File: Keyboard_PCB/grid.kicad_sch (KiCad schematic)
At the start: 136 parts, among them SW10 7, SW11 8, SW12 9, SW13 0, SW14 -, SW15 =, SW16 <-, SW17 DEL, SW18 TAB, SW19 Q, SW20 W, SW21 E, SW22 R, SW23 T, SW24 Y, SW25 U, SW26 I, SW27 O, SW28 P, SW29 [, SW3 ESC, SW30 ], SW31 \, SW32 HOME, SW34 CAPS, SW35 A, SW36 S, SW37 D, SW38 F, SW39 G, SW4 1, SW40 H, SW41 J, SW42 K, SW43 L, SW44 ;, SW45 ', SW46 ENTER, SW47 PG_U, SW48 SHIFT, SW49 Z, SW5 2, SW50 X, SW51 C, SW52 V, SW53 B, SW54 N, SW55 M, SW56 ,, SW57 ., SW58 /, SW59 SHIFT, SW6 3, SW60 UP, SW61 PG_D, SW62 CTRL, SW63 CODE, SW64 ALT, SW65 SPACE, SW66 ALT, SW67 CODE, SW68 CTRL, SW69 LEFT, SW7 4, SW70 DOWN, SW71 RIGHT, SW8 5, SW9 6

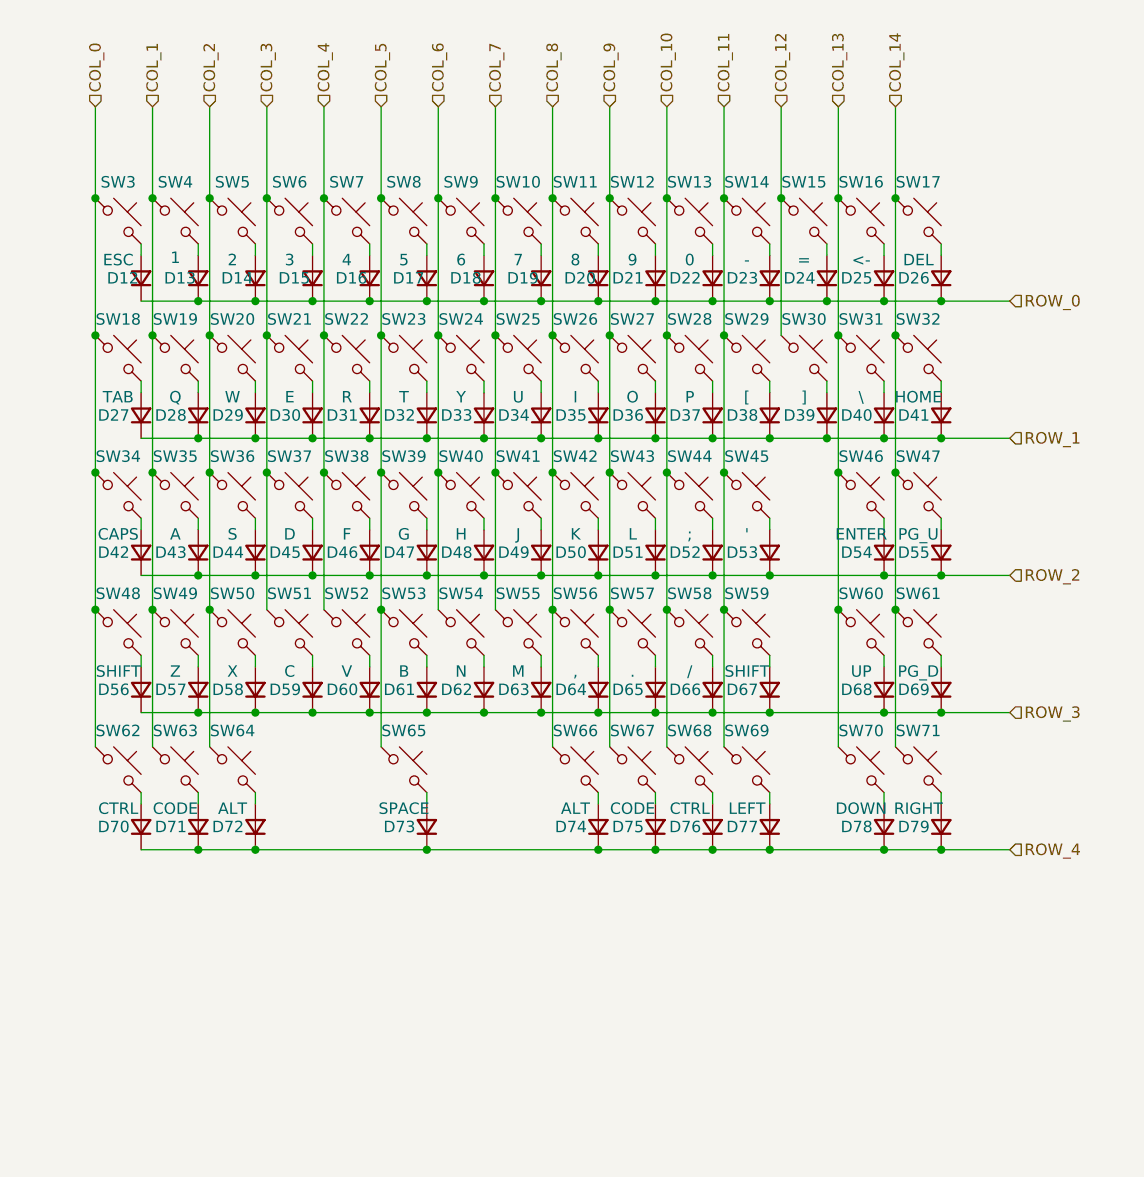
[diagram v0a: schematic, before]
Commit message: Keypad schematic progress
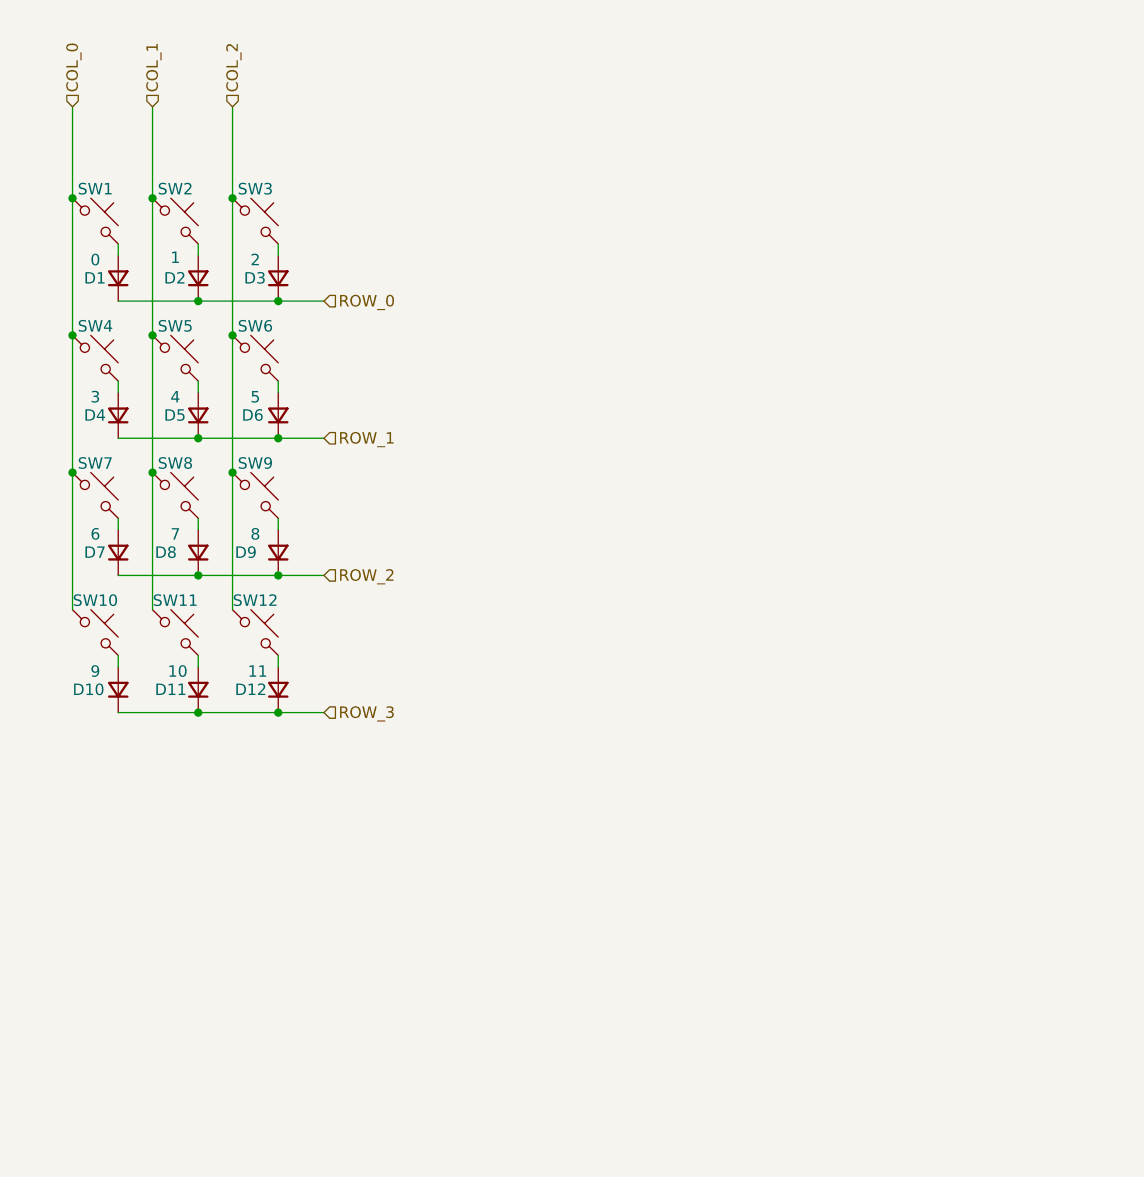
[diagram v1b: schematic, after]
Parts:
- removed D15, D16, D17, D18, D19, D20, D21, D22, D23, D24, D25, D26, D30, D31, D32, D33, D34, D35, D36, D37, D38, D39, D40, D41, D45, D46, D47, D48, D49, D50, D51, D52, D53, D54, D55, D59, D60, D61, D62, D63, D64, D65, D66, D67, D68, D69, D70, D71, D72, D73, D74, D75, D76, D77, D78, D79: D_Small, Diode_SMD:D_SOD-323, symbol Device:D_Small
- removed SW10: 7, Keyboard_Switch:SW_Cherry_MX1A_1.00u_PCB, symbol Switch:SW_Push_45deg
- removed SW11: 8, Keyboard_Switch:SW_Cherry_MX1A_1.00u_PCB, symbol Switch:SW_Push_45deg
- removed SW12: 9, Keyboard_Switch:SW_Cherry_MX1A_1.00u_PCB, symbol Switch:SW_Push_45deg
- removed SW13: 0, Keyboard_Switch:SW_Cherry_MX1A_1.00u_PCB, symbol Switch:SW_Push_45deg
- removed SW14: -, Keyboard_Switch:SW_Cherry_MX1A_1.00u_PCB, symbol Switch:SW_Push_45deg
- removed SW15: =, Keyboard_Switch:SW_Cherry_MX1A_1.00u_PCB, symbol Switch:SW_Push_45deg
- removed SW16: <-, Keyboard_Switch:SW_Cherry_MX1A_2.00u_PCB, symbol Switch:SW_Push_45deg
- removed SW17: DEL, Keyboard_Switch:SW_Cherry_MX1A_1.00u_PCB, symbol Switch:SW_Push_45deg
- removed SW21: E, Keyboard_Switch:SW_Cherry_MX1A_1.00u_PCB, symbol Switch:SW_Push_45deg
- removed SW22: R, Keyboard_Switch:SW_Cherry_MX1A_1.00u_PCB, symbol Switch:SW_Push_45deg
- removed SW23: T, Keyboard_Switch:SW_Cherry_MX1A_1.00u_PCB, symbol Switch:SW_Push_45deg
- removed SW24: Y, Keyboard_Switch:SW_Cherry_MX1A_1.00u_PCB, symbol Switch:SW_Push_45deg
- removed SW25: U, Keyboard_Switch:SW_Cherry_MX1A_1.00u_PCB, symbol Switch:SW_Push_45deg
- removed SW26: I, Keyboard_Switch:SW_Cherry_MX1A_1.00u_PCB, symbol Switch:SW_Push_45deg
- removed SW27: O, Keyboard_Switch:SW_Cherry_MX1A_1.00u_PCB, symbol Switch:SW_Push_45deg
- removed SW28: P, Keyboard_Switch:SW_Cherry_MX1A_1.00u_PCB, symbol Switch:SW_Push_45deg
- removed SW29: [, Keyboard_Switch:SW_Cherry_MX1A_1.00u_PCB, symbol Switch:SW_Push_45deg
- removed SW30: ], Keyboard_Switch:SW_Cherry_MX1A_1.00u_PCB, symbol Switch:SW_Push_45deg
- removed SW31: \, Keyboard_Switch:SW_Cherry_MX1A_1.50u_PCB, symbol Switch:SW_Push_45deg
- removed SW32: HOME, Keyboard_Switch:SW_Cherry_MX1A_1.00u_PCB, symbol Switch:SW_Push_45deg
- removed SW37: D, Keyboard_Switch:SW_Cherry_MX1A_1.00u_PCB, symbol Switch:SW_Push_45deg
- removed SW38: F, Keyboard_Switch:SW_Cherry_MX1A_1.00u_PCB, symbol Switch:SW_Push_45deg
- removed SW39: G, Keyboard_Switch:SW_Cherry_MX1A_1.00u_PCB, symbol Switch:SW_Push_45deg
- removed SW40: H, Keyboard_Switch:SW_Cherry_MX1A_1.00u_PCB, symbol Switch:SW_Push_45deg
- removed SW41: J, Keyboard_Switch:SW_Cherry_MX1A_1.00u_PCB, symbol Switch:SW_Push_45deg
- removed SW42: K, Keyboard_Switch:SW_Cherry_MX1A_1.00u_PCB, symbol Switch:SW_Push_45deg
- removed SW43: L, Keyboard_Switch:SW_Cherry_MX1A_1.00u_PCB, symbol Switch:SW_Push_45deg
- removed SW44: ;, Keyboard_Switch:SW_Cherry_MX1A_1.00u_PCB, symbol Switch:SW_Push_45deg
- removed SW45: ', Keyboard_Switch:SW_Cherry_MX1A_1.00u_PCB, symbol Switch:SW_Push_45deg
- removed SW46: ENTER, Keyboard_Switch:SW_Cherry_MX1A_2.25u_PCB, symbol Switch:SW_Push_45deg
- removed SW47: PG_U, Keyboard_Switch:SW_Cherry_MX1A_1.00u_PCB, symbol Switch:SW_Push_45deg
- removed SW51: C, Keyboard_Switch:SW_Cherry_MX1A_1.00u_PCB, symbol Switch:SW_Push_45deg
- removed SW52: V, Keyboard_Switch:SW_Cherry_MX1A_1.00u_PCB, symbol Switch:SW_Push_45deg
- removed SW53: B, Keyboard_Switch:SW_Cherry_MX1A_1.00u_PCB, symbol Switch:SW_Push_45deg
- removed SW54: N, Keyboard_Switch:SW_Cherry_MX1A_1.00u_PCB, symbol Switch:SW_Push_45deg
- removed SW55: M, Keyboard_Switch:SW_Cherry_MX1A_1.00u_PCB, symbol Switch:SW_Push_45deg
- removed SW56: ,, Keyboard_Switch:SW_Cherry_MX1A_1.00u_PCB, symbol Switch:SW_Push_45deg
- removed SW57: ., Keyboard_Switch:SW_Cherry_MX1A_1.00u_PCB, symbol Switch:SW_Push_45deg
- removed SW58: /, Keyboard_Switch:SW_Cherry_MX1A_1.00u_PCB, symbol Switch:SW_Push_45deg
- removed SW59: SHIFT, Keyboard_Switch:SW_Cherry_MX1A_1.75u_PCB, symbol Switch:SW_Push_45deg
- removed SW6: 3, Keyboard_Switch:SW_Cherry_MX1A_1.00u_PCB, symbol Switch:SW_Push_45deg
- removed SW60: UP, Keyboard_Switch:SW_Cherry_MX1A_1.00u_PCB, symbol Switch:SW_Push_45deg
- removed SW61: PG_D, Keyboard_Switch:SW_Cherry_MX1A_1.00u_PCB, symbol Switch:SW_Push_45deg
- removed SW62: CTRL, Keyboard_Switch:SW_Cherry_MX1A_1.25u_PCB, symbol Switch:SW_Push_45deg
- removed SW63: CODE, Keyboard_Switch:SW_Cherry_MX1A_1.25u_PCB, symbol Switch:SW_Push_45deg
- removed SW64: ALT, Keyboard_Switch:SW_Cherry_MX1A_1.25u_PCB, symbol Switch:SW_Push_45deg
- removed SW65: SPACE, Keyboard_Switch:SW_Cherry_MX1A_6.25u_PCB, symbol Switch:SW_Push_45deg
- removed SW66: ALT, Keyboard_Switch:SW_Cherry_MX1A_1.00u_PCB, symbol Switch:SW_Push_45deg
- removed SW67: CODE, Keyboard_Switch:SW_Cherry_MX1A_1.00u_PCB, symbol Switch:SW_Push_45deg
- removed SW68: CTRL, Keyboard_Switch:SW_Cherry_MX1A_1.00u_PCB, symbol Switch:SW_Push_45deg
- removed SW69: LEFT, Keyboard_Switch:SW_Cherry_MX1A_1.00u_PCB, symbol Switch:SW_Push_45deg
- removed SW7: 4, Keyboard_Switch:SW_Cherry_MX1A_1.00u_PCB, symbol Switch:SW_Push_45deg
- removed SW70: DOWN, Keyboard_Switch:SW_Cherry_MX1A_1.00u_PCB, symbol Switch:SW_Push_45deg
- removed SW71: RIGHT, Keyboard_Switch:SW_Cherry_MX1A_1.00u_PCB, symbol Switch:SW_Push_45deg
- removed SW8: 5, Keyboard_Switch:SW_Cherry_MX1A_1.00u_PCB, symbol Switch:SW_Push_45deg
- removed SW9: 6, Keyboard_Switch:SW_Cherry_MX1A_1.00u_PCB, symbol Switch:SW_Push_45deg
- SW1: renamed from SW3; value ESC -> 0; footprint Keyboard_Switch:SW_Cherry_MX1A_1.00u_PCB -> Button_Switch_Keyboard:SW_Cherry_MX_1.00u_PCB
- SW10: renamed from SW48; value SHIFT -> 9; footprint Keyboard_Switch:SW_Cherry_MX1A_2.25u_PCB -> Button_Switch_Keyboard:SW_Cherry_MX_1.00u_PCB
- SW11: renamed from SW49; value Z -> 10; footprint Keyboard_Switch:SW_Cherry_MX1A_1.00u_PCB -> Button_Switch_Keyboard:SW_Cherry_MX_1.00u_PCB
- SW12: renamed from SW50; value X -> 11; footprint Keyboard_Switch:SW_Cherry_MX1A_1.00u_PCB -> Button_Switch_Keyboard:SW_Cherry_MX_1.00u_PCB
- SW2: renamed from SW4; footprint Keyboard_Switch:SW_Cherry_MX1A_1.00u_PCB -> Button_Switch_Keyboard:SW_Cherry_MX_1.00u_PCB
- SW3: renamed from SW5; footprint Keyboard_Switch:SW_Cherry_MX1A_1.00u_PCB -> Button_Switch_Keyboard:SW_Cherry_MX_1.00u_PCB
- SW4: renamed from SW18; value TAB -> 3; footprint Keyboard_Switch:SW_Cherry_MX1A_1.50u_PCB -> Button_Switch_Keyboard:SW_Cherry_MX_1.00u_PCB
- SW5: renamed from SW19; value Q -> 4; footprint Keyboard_Switch:SW_Cherry_MX1A_1.00u_PCB -> Button_Switch_Keyboard:SW_Cherry_MX_1.00u_PCB
- SW6: renamed from SW20; value W -> 5; footprint Keyboard_Switch:SW_Cherry_MX1A_1.00u_PCB -> Button_Switch_Keyboard:SW_Cherry_MX_1.00u_PCB
- SW7: renamed from SW34; value CAPS -> 6; footprint Keyboard_Switch:SW_Cherry_MX1A_1.75u_PCB -> Button_Switch_Keyboard:SW_Cherry_MX_1.00u_PCB
- SW8: renamed from SW35; value A -> 7; footprint Keyboard_Switch:SW_Cherry_MX1A_1.00u_PCB -> Button_Switch_Keyboard:SW_Cherry_MX_1.00u_PCB
- SW9: renamed from SW36; value S -> 8; footprint Keyboard_Switch:SW_Cherry_MX1A_1.00u_PCB -> Button_Switch_Keyboard:SW_Cherry_MX_1.00u_PCB
- renumbered D12 to D1, D56 to D10, D57 to D11, D58 to D12, D13 to D2, D14 to D3, D27 to D4, D28 to D5, D29 to D6, D42 to D7, D43 to D8, D44 to D9
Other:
- moved on the sheet: D1, D10, D12, D3, D4, D6, D7, D9, SW1, SW10, SW12, SW3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

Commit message: STM32U385 pin assignment progress
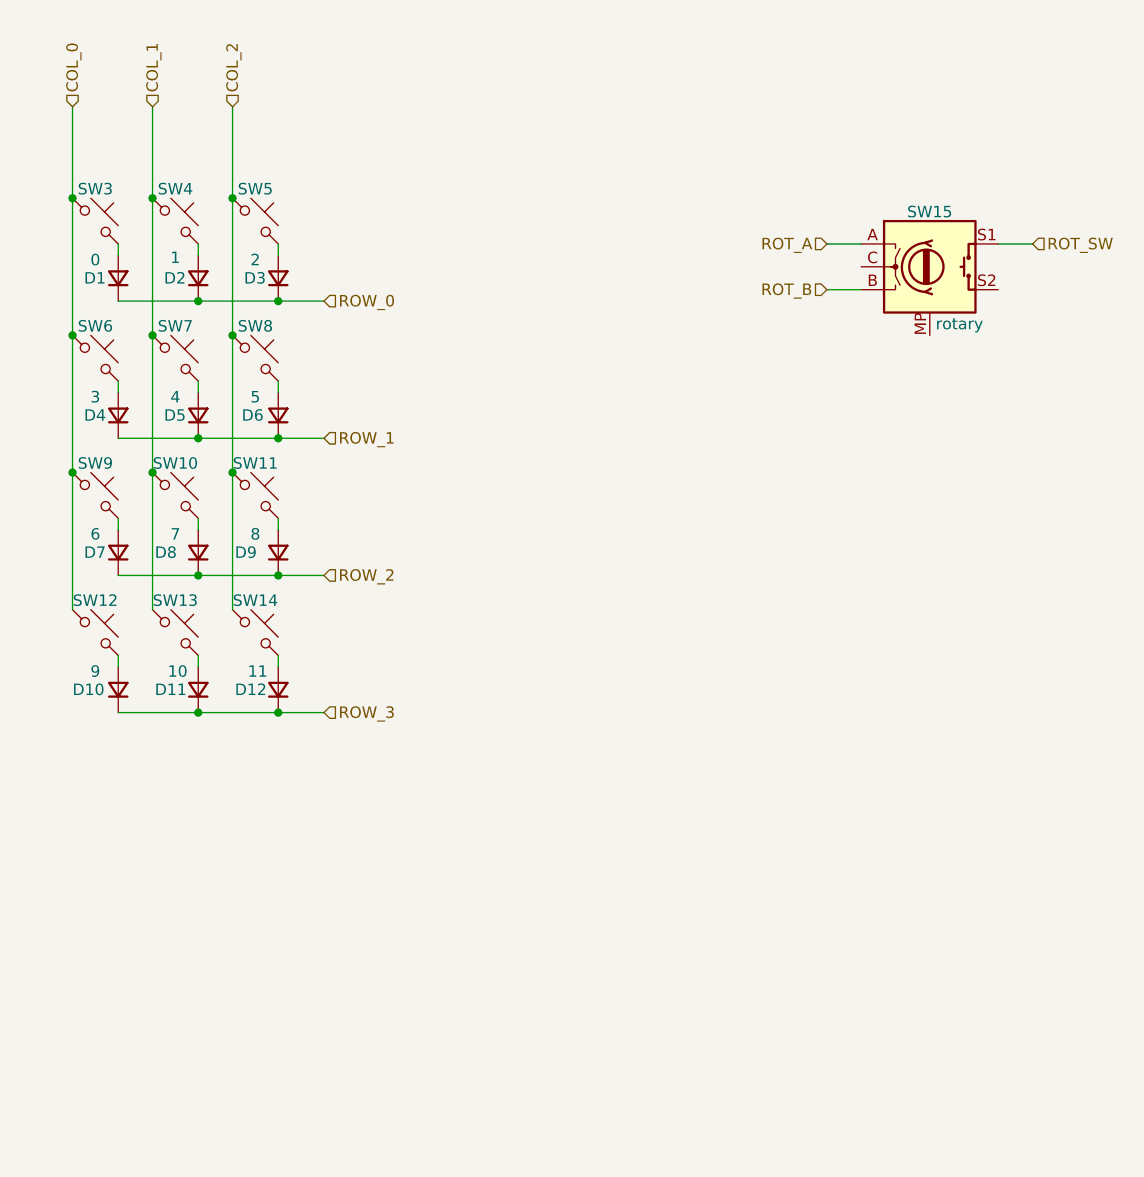
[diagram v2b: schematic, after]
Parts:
- added SW15: rotary, symbol Device:RotaryEncoder_Switch_MP
- renumbered SW8 to SW10, SW9 to SW11, SW10 to SW12, SW11 to SW13, SW12 to SW14, SW1 to SW3, SW2 to SW4, SW3 to SW5, SW4 to SW6, SW5 to SW7, SW6 to SW8, SW7 to SW9
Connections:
- new net ROT_A: SW15.A
- new net ROT_B: SW15.B
- new net ROT_SW: SW15.S1
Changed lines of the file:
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@@
+	(wire
+		(pts
+			(xy 167.64 66.04) (xy 163.83 66.04)
+		)
+		(stroke
+			(width 0)
+			(type default)
+		)
+	)
 	(wire
 		(pts
@@
 	(wire
 		(pts
+			(xy 144.78 71.12) (xy 148.59 71.12)
+		)
+		(stroke
+			(width 0)
+			(type default)
+		)
+	)
+	(wire
+		(pts
 			(xy 60.96 60.96) (xy 60.96 76.2)
 		)
@@
 	(wire
 		(pts
+			(xy 144.78 66.04) (xy 148.59 66.04)
+		)
+		(stroke
+			(width 0)
+			(type default)
+		)
+	)
+	(wire
+		(pts
 			(xy 83.82 67.31) (xy 83.82 66.04)
 		)
@@
 			(width 0)
 			(type default)
+		)
+	)
+	(hierarchical_label "ROT_B"
+		(shape input)
+		(at 144.78 71.12 180)
+		(effects
+			(font
+				(size 1.27 1.27)
+			)
+			(justify right)
 		)
 	)
@@
 		)
 	)
+	(hierarchical_label "ROT_SW"
+		(shape input)
+		(at 167.64 66.04 0)
+		(effects
+			(font
+				(size 1.27 1.27)
+			)
+			(justify left)
+		)
+	)
+	(hierarchical_label "ROT_A"
+		(shape input)
+		(at 144.78 66.04 180)
+		(effects
+			(font
+				(size 1.27 1.27)
+			)
+			(justify right)
+		)
+	)
 	(hierarchical_label "ROW_3"
 		(shape input)
@@
 		(on_board yes)
 		(dnp no)
-		(property "Reference" "SW4"
+		(property "Reference" "SW6"
 			(at 63.5 75.184 0)
 			(effects
@@
 			(project "Keyboard_PCB"
 				(path "/dd51e792-c76c-4d43-96de-494177f3b593/2efb7614-f68d-465d-9514-3e61f2b99fcc"
-					(reference "SW4")
+					(reference "SW6")
 					(unit 1)
 				)
@@
 		(on_board yes)
 		(dnp no)
-		(property "Reference" "SW12"
+		(property "Reference" "SW14"
 			(at 81.28 105.664 0)
 			(effects
@@
 			(project "Keyboard_PCB"
 				(path "/dd51e792-c76c-4d43-96de-494177f3b593/2efb7614-f68d-465d-9514-3e61f2b99fcc"
-					(reference "SW12")
+					(reference "SW14")
 					(unit 1)
 				)
@@
 		(on_board yes)
 		(dnp no)
-		(property "Reference" "SW5"
+		(property "Reference" "SW7"
 			(at 72.39 75.184 0)
 			(effects
@@
 			(project "Keyboard_PCB"
 				(path "/dd51e792-c76c-4d43-96de-494177f3b593/2efb7614-f68d-465d-9514-3e61f2b99fcc"
-					(reference "SW5")
+					(reference "SW7")
 					(unit 1)
 				)
@@
 		(on_board yes)
 		(dnp no)
-		(property "Reference" "SW3"
+		(property "Reference" "SW5"
 			(at 81.28 59.944 0)
 			(effects
@@
 			(project "Keyboard_PCB"
 				(path "/dd51e792-c76c-4d43-96de-494177f3b593/2efb7614-f68d-465d-9514-3e61f2b99fcc"
-					(reference "SW3")
+					(reference "SW5")
 					(unit 1)
 				)
@@
 		(on_board yes)
 		(dnp no)
-		(property "Reference" "SW7"
+		(property "Reference" "SW9"
 			(at 63.5 90.424 0)
 			(effects
@@
 			(project "Keyboard_PCB"
 				(path "/dd51e792-c76c-4d43-96de-494177f3b593/2efb7614-f68d-465d-9514-3e61f2b99fcc"
-					(reference "SW7")
+					(reference "SW9")
 					(unit 1)
 				)
@@
 		(on_board yes)
 		(dnp no)
-		(property "Reference" "SW9"
+		(property "Reference" "SW11"
 			(at 81.28 90.424 0)
 			(effects
@@
 			(project "Keyboard_PCB"
 				(path "/dd51e792-c76c-4d43-96de-494177f3b593/2efb7614-f68d-465d-9514-3e61f2b99fcc"
-					(reference "SW9")
+					(reference "SW11")
 					(unit 1)
 				)
@@
 		(on_board yes)
 		(dnp no)
-		(property "Reference" "SW1"
+		(property "Reference" "SW3"
 			(at 63.5 59.944 0)
 			(effects
@@
 			(project "Keyboard_PCB"
 				(path "/dd51e792-c76c-4d43-96de-494177f3b593/2efb7614-f68d-465d-9514-3e61f2b99fcc"
-					(reference "SW1")
+					(reference "SW3")
 					(unit 1)
 				)
@@
 		(on_board yes)
 		(dnp no)
-		(property "Reference" "SW6"
+		(property "Reference" "SW8"
 			(at 81.28 75.184 0)
 			(effects
@@
 			(project "Keyboard_PCB"
 				(path "/dd51e792-c76c-4d43-96de-494177f3b593/2efb7614-f68d-465d-9514-3e61f2b99fcc"
-					(reference "SW6")
+					(reference "SW8")
 					(unit 1)
 				)
@@
 		(on_board yes)
 		(dnp no)
-		(property "Reference" "SW10"
+		(property "Reference" "SW12"
 			(at 63.5 105.664 0)
 			(effects
@@
 			(project "Keyboard_PCB"
 				(path "/dd51e792-c76c-4d43-96de-494177f3b593/2efb7614-f68d-465d-9514-3e61f2b99fcc"
-					(reference "SW10")
+					(reference "SW12")
 					(unit 1)
 				)
@@
 		(on_board yes)
 		(dnp no)
-		(property "Reference" "SW8"
+		(property "Reference" "SW10"
 			(at 72.39 90.424 0)
 			(effects
@@
 			(project "Keyboard_PCB"
 				(path "/dd51e792-c76c-4d43-96de-494177f3b593/2efb7614-f68d-465d-9514-3e61f2b99fcc"
-					(reference "SW8")
+					(reference "SW10")
 					(unit 1)
 				)
@@
 		(on_board yes)
 		(dnp no)
-		(property "Reference" "SW11"
+		(property "Reference" "SW13"
 			(at 72.39 105.664 0)
 			(effects
@@
 			(project "Keyboard_PCB"
 				(path "/dd51e792-c76c-4d43-96de-494177f3b593/2efb7614-f68d-465d-9514-3e61f2b99fcc"
-					(reference "SW11")
+					(reference "SW13")
 					(unit 1)
 				)
@@
 		(on_board yes)
 		(dnp no)
-		(property "Reference" "SW2"
+		(property "Reference" "SW4"
 			(at 72.39 59.944 0)
 			(effects
@@
 			(project "Keyboard_PCB"
 				(path "/dd51e792-c76c-4d43-96de-494177f3b593/2efb7614-f68d-465d-9514-3e61f2b99fcc"
-					(reference "SW2")
-					(unit 1)
-				)
+					(reference "SW4")
+					(unit 1)
+				)
+			)
+		)
+	)
+	(symbol
+		(lib_id "Device:RotaryEncoder_Switch_MP")
+		(at 156.21 68.58 0)
+		(unit 1)
+		(exclude_from_sim no)
+		(in_bom yes)
+		(on_board yes)
+		(dnp no)
+		(property "Reference" "SW15"
+			(at 156.21 62.484 0)
+			(effects
+				(font
+					(size 1.27 1.27)
+				)
+			)
+		)
+		(property "Value" "rotary"
+			(at 159.512 74.93 0)
+			(effects
+				(font
+					(size 1.27 1.27)
+				)
+			)
+		)
+		(property "Footprint" ""
+			(at 152.4 64.516 0)
+			(effects
+				(font
+					(size 1.27 1.27)
+				)
+				(hide yes)
+			)
+		)
+		(property "Datasheet" "~"
+			(at 156.21 81.28 0)
+			(effects
+				(font
+					(size 1.27 1.27)
+				)
+				(hide yes)
+			)
+		)
+		(property "Description" "Rotary encoder, dual channel, incremental quadrate outputs, with switch and MP Pin"
+			(at 156.21 83.82 0)
+			(effects
+				(font
+					(size 1.27 1.27)
+				)
+				(hide yes)
+			)
+		)
+		(pin "B"
+		)
+		(pin "MP"
+		)
+		(pin "S1"
+		)
+		(pin "A"
+		)
+		(pin "S2"
+		)
+		(pin "C"
+		)
+		(instances
+			(project "Keyboard_PCB"
+				(path "/dd51e792-c76c-4d43-96de-494177f3b593/2efb7614-f68d-465d-9514-3e61f2b99fcc"
+					(reference "SW15")
+					(unit 1)
+				)
